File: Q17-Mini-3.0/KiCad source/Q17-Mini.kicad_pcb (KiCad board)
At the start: 2 copper layers, 95 x 75 mm, 89 parts, among them J1 INPUT, J2-1 SPK+, J2-2 SPK-, J3-1 V+, J3-2 GND, J3-3 V-, J4 PinHeader_1x01_P1.27mm_Vertic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, Q1 IRF610, Q10 KSA992, Q11 BS250P, Q111 BS250P, Q12 KSC1845, Q13 IRF610, Q14 IRF9610, Q15 FQA46N15, Q16 IXTH48P20P, Q2 KSA992, Q3 KSC1845, Q4 IRF9610, Q5 FQPF7P20, Q6 2SK3564, Q7 LSK170B, Q7' DN2540N8-G, Q8 DN2540, Q9 BS250P, U1 OPA1611, U1' OPA1611, U2 NDC7003P

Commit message: Update Q17-Mini diagram
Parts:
- R15: value 330R -> 150R
- R17: value 5k1 -> 4k75
- R6: value 100R/0.5W -> 196R/0.5W
- R7: value 100R -> 120R
- R8: value 120R -> 100R
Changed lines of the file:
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@@
 	(title_block
 		(title "Q17-Mini, the Quad405 reborn")
-		(date "2024-07-01")
+		(date "2024-07-28")
 		(rev "3.0.1")
 		(company "PCB design by Stef")
@@
 			)
 		)
-		(property "Value" "100R/0.5W"
+		(property "Value" "196R/0.5W"
 			(at 5.08 2.37 0)
 			(layer "F.Fab")
@@
 			)
 		)
-		(property "Mouser" "594-MRS25000C1000FCT"
+		(property "Mouser" "594-MRS25000C1960FCT"
 			(at 0 0 0)
 			(layer "F.Fab")
@@
 			)
 		)
-		(property "Part#" "MRS25000C1000FC100"
+		(property "Part#" "MRS25000C1960FCT00"
 			(at 0 0 0)
 			(layer "F.Fab")
@@
 			)
 		)
-		(property "Value" "120R"
+		(property "Value" "100R"
 			(at 5.08 2.37 90)
 			(layer "F.Fab")
@@
 			)
 		)
-		(property "Mouser" "594-MRS25000C1200FCT"
+		(property "Mouser" "594-MRS25000C1000FCT"
 			(at 0 0 0)
 			(layer "F.Fab")
@@
 			)
 		)
-		(property "Part#" "MRS25000C1200FCT00"
+		(property "Part#" "MRS25000C1000FCT00"
 			(at 0 0 0)
 			(layer "F.Fab")
@@
 			)
 		)
-		(property "Datasheet" "https://www.mouser.fr/datasheet/2/240/ixyss09010_1-2272779.pdf"
+		(property "Datasheet" "https://www.mouser.fr/datasheet/2/240/media-3323106.pdf"
 			(at 0 0 -90)
 			(unlocked yes)
@@
 			)
 		)
-		(property "Value" "330R"
+		(property "Value" "150R"
 			(at 12.7 1.25 90)
 			(layer "F.Fab")
@@
 			)
 		)
-		(property "Mouser" "594-MRS25000C3300FCT"
+		(property "Mouser" "594-MRS25000C1500FRP"
 			(at 0 0 0)
 			(layer "F.Fab")
@@
 			)
 		)
-		(property "Part#" "MRS25000C3300FCT00"
+		(property "Part#" "MRS25000C1500FRP00"
 			(at 0 0 0)
 			(layer "F.Fab")
@@
 			)
 		)
-		(property "Value" "100R"
+		(property "Value" "120R"
 			(at 5.08 2.37 90)
 			(layer "F.Fab")
@@
 			)
 		)
-		(property "Mouser" "594-MRS25000C1000FCT"
+		(property "Mouser" "594-MRS25000C1200FCT"
 			(at 0 0 180)
 			(layer "F.Fab")
@@
 			)
 		)
-		(property "Part#" "MRS25000C1000FCT00"
+		(property "Part#" "MRS25000C1200FCT00"
 			(at 0 0 180)
 			(layer "F.Fab")
@@
 			)
 		)
-		(property "Value" "5k1"
+		(property "Value" "4k75"
 			(at 5.08 2.37 180)
 			(layer "F.Fab")
@@
 			)
 		)
-		(property "Description" "5k1 resistor"
+		(property "Description" ""
 			(at 0 0 180)
 			(unlocked yes)
@@
 			)
 		)
-		(property "Mouser" "594-MRS25000C5101FRP"
+		(property "Mouser" "594-MRS25000C4751FRP"
 			(at 0 0 -90)
 			(layer "F.Fab")
@@
 			)
 		)
-		(property "Part#" "MRS25000C5101FRP00"
+		(property "Part#" "MRS25000C4751FRP00"
 			(at 0 0 -90)
 			(layer "F.Fab")

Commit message: Upload Q17-Mini 3.0.2
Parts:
- removed J4: PinHeader_1x01_P1.27mm_Vertical, Connector_PinHeader_1.27mm:PinHeader_1x01_P1.27mm_Vertical
- added D8: SL1M-AQ, Diode_SMD:D_SOD-123, F.Cu at (193.2, 88.0)
- added D9: SL1M-AQ, Diode_SMD:D_SOD-123, F.Cu at (193.2, 97.0)
- added Q1': SI2328DS, Package_TO_SOT_SMD:SOT-23_Handsoldering, B.Cu at (108.4, 66.3)
- added Q4': SI2325DS, Package_TO_SOT_SMD:SOT-23_Handsoldering, B.Cu at (107.1, 121.3)
- Q16: value IXTH48P20P -> IXTQ36P15P
- Q7': value DN2540N8-G -> JFE150
- R10, R13: value 9R1 -> 8R2
- R15: value 150R -> 330R
- R7: value 120R -> 100R
- moved Q7' 13.3 mm to (126.2, 75.6), turned to -90 degrees
- moved D10 2.06 mm to (193.2, 110.2)
- moved R31 0.78 mm to (142.9, 99.0)
- renumbered D8 to D10
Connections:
- D10 pad 1: Net-(D7-A) -> Net-(D10-K)
- L1 pad 1: Net-(D7-A) -> Net-(D8-K)
- Q15 pad 3: Net-(D7-A) -> Net-(D8-K)
- Q16 pad 3: Net-(D7-A) -> Net-(D8-K)
- R27 pad 2: Net-(D7-A) -> Net-(D8-K)
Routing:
- net Net-(D7-A): track 107.8 -> 9.53 mm
- net Net-(D8-K): track 0.00 -> 83.4 mm
- net Net-(Q4-S): track 37.7 -> 50.0 mm
- net Net-(Q7-D): track 16.2 -> 5.61 mm
- net Net-(Q7-S): track 42.6 -> 32.1 mm
- net Net-(D10-K): track 0.00 -> 9.86 mm
- net Net-(D1-A): track 91.8 -> 101.2 mm
- net Net-(Q4-G): track 5.19 -> 10.2 mm
- net Net-(Q7-G): track 25.0 -> 29.9 mm
- net Net-(U2-S1): track 23.9 -> 20.1 mm
- net Net-(D4-K): track 89.8 -> 92.9 mm
- net Net-(Q1-G): track 4.92 -> 7.98 mm
- net Net-(D10-A): track 31.6 -> 29.6 mm
- net Net-(Q1-S): track 35.1 -> 36.7 mm
- net Net-(C17-Pad1): track 14.2 -> 13.4 mm
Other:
- board text added: "D"
- board text added: "G"
- board text added: "Q17-Mini 3.0.2"
- board text added: "S"
- board text removed: "Q17-Mini 3.0.1"

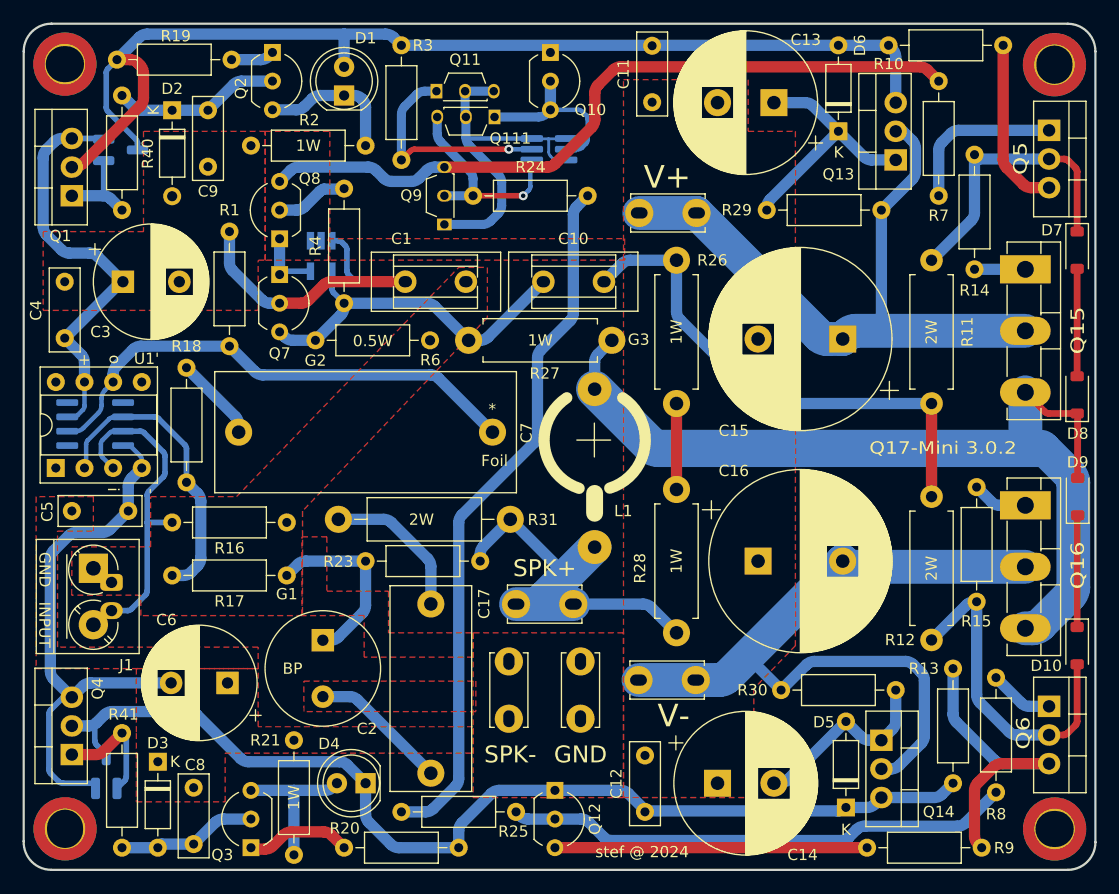
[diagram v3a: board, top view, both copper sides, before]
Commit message: Update Q17-Mini to 3.0.3
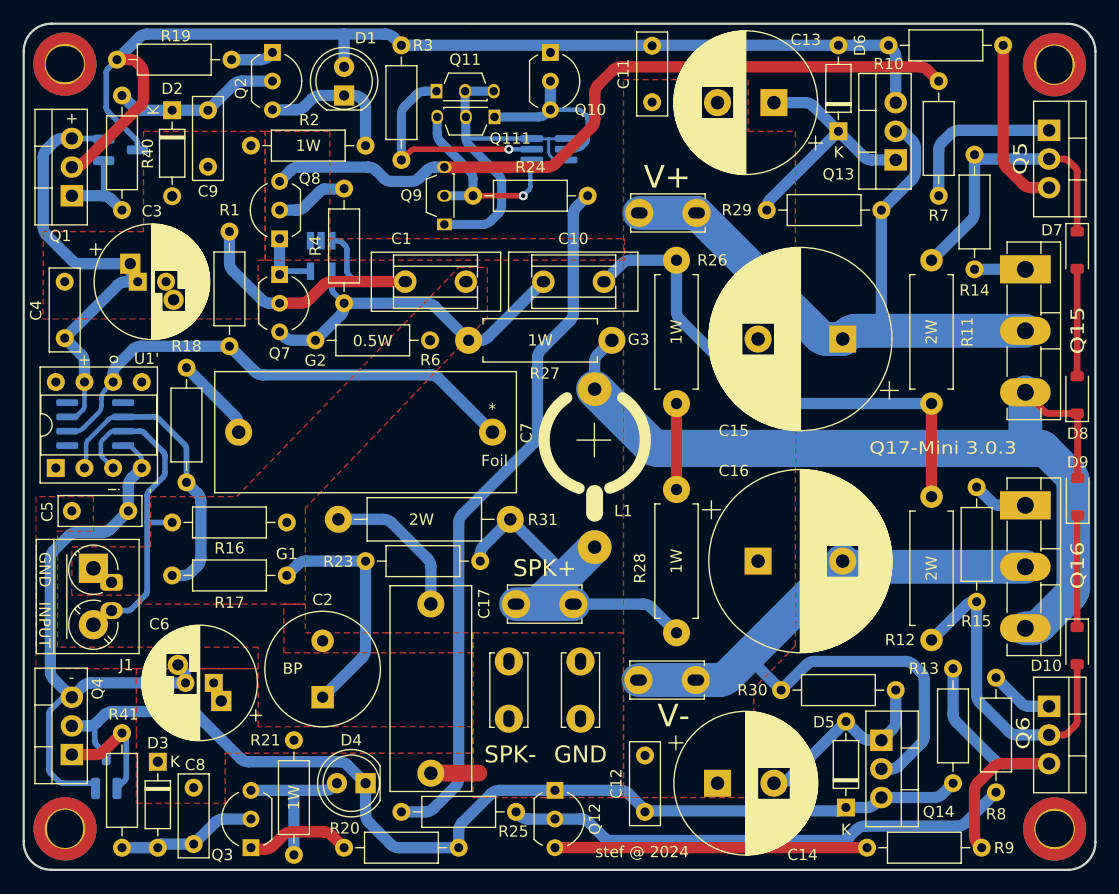
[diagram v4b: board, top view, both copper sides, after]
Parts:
- C3, C6: footprint Capacitor_THT:CP_Radial_D10.0mm_P5.00mm -> Capacitor_THT:CP_Radial_D10.0mm_P2.50mm_P5.00mm
- C7: value 2.2uF MKP or FKP -> 2.2uF MKP
- R15: value 330R -> 270R
- moved C2 5.05 mm to (126.3, 114.8), turned to 90 degrees
- moved C3 1.32 mm to (109.9, 77.9)
- moved C6 1.22 mm to (116.7, 113.5)
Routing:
- net GND: track 12.3 -> 4.25 mm
- net Net-(C2-Pad1): track 16.6 -> 21.1 mm
- net Net-(Q1-S): track 36.7 -> 40.0 mm
- net Net-(Q4-S): track 50.0 -> 53.1 mm
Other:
- board text added: "Q17-Mini 3.0.3"
- board text removed: "Q17-Mini 3.0.2"
